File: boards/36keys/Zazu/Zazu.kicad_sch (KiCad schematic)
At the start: 169 parts, among them J1 Conn_01x12_Female, J2 Conn_01x12_Female, J3 Conn_01x08_Female, J4 Conn_01x08_Female, J5 Conn_01x03_Female, SW1 SW_Push, SW10 SW_Push, SW11 SW_Push, SW12 SW_Push, SW13 SW_Push, SW14 SW_Push, SW15 SW_Push, SW16 SW_Push, SW17 SW_Push, SW18 SW_Push, SW19 SW_Push, SW2 SW_Push, SW20 SW_Push, SW21 SW_Push, SW22 SW_Push, SW23 SW_Push, SW24 SW_Push, SW25 SW_Push, SW26 SW_Push, SW27 SW_Push, SW28 SW_Push, SW29 SW_Push, SW3 SW_Push, SW30 SW_Push, SW31 SW_Push, SW32 SW_Push, SW33 SW_Push, SW34 SW_Push, SW35 SW_Push, SW36 RotaryEncoder, SW37 SW_SPDT, SW38 SW_Push, SW39 SW_Push, SW4 SW_Push, SW40 SW_Push, SW41 SW_Push, SW42 SW_Push, SW43 SW_Push, SW44 SW_Push, SW45 SW_Push, SW46 SW_Push, SW5 SW_Push, SW6 SW_Push, SW7 SW_Push, SW8 SW_Push, SW9 SW_Push, U1 Elite-C, U2 74HC595, U3 TCR2EF19,LM(CT, U4 PMW3360DM-T2QU, U5 DRV2605L

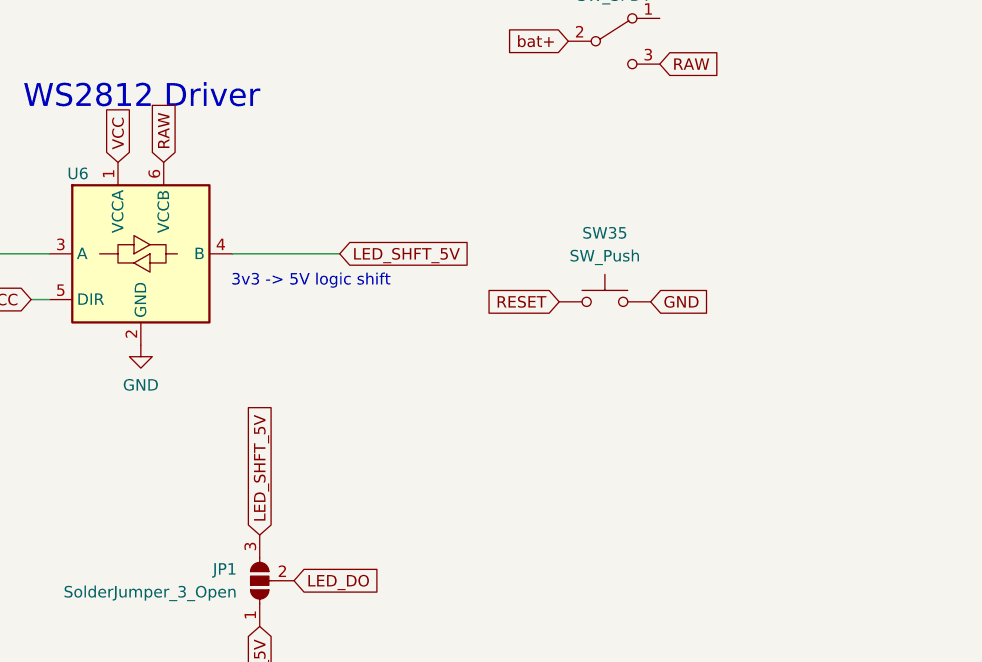
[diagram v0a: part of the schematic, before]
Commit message: change Zazu's reset switch
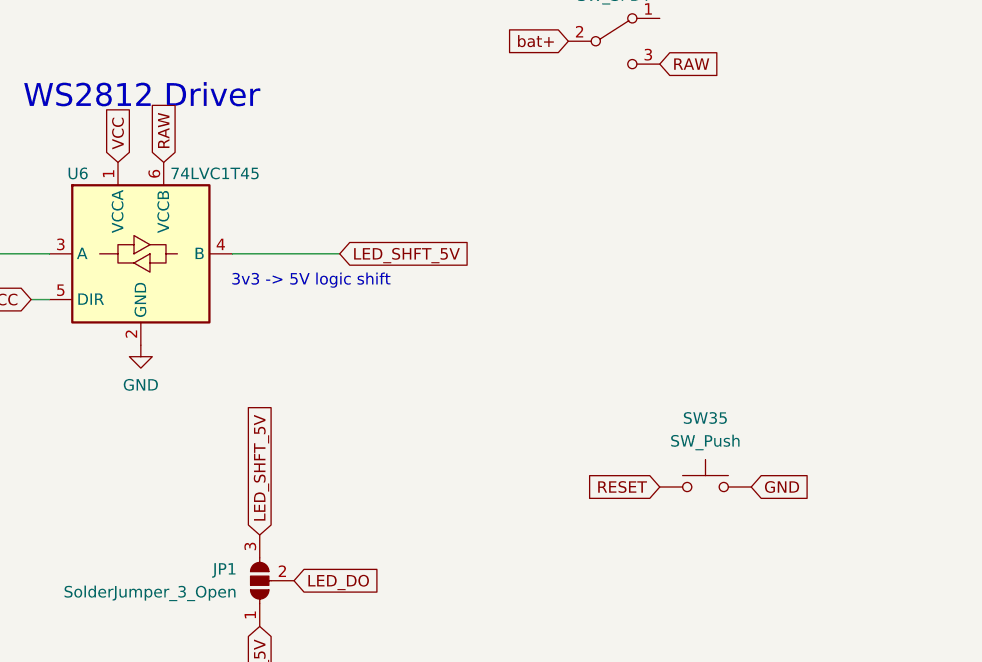
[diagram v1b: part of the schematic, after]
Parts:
- SW35: footprint Button_Switch_SMD:SW_SPST_Omron_B3FS-100xP -> Alaa:SKQG-1155865; LCSC C271750 -> C221856
- U6: value (none) -> 74LVC1T45; footprint (none) -> Package_TO_SOT_SMD:SOT-363_SC-70-6
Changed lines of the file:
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@@
     )
   )
+  (global_label "RESET" (shape input) (at 384.81 257.556 180) (fields_autoplaced)
+    (effects (font (size 1.27 1.27)) (justify right))
+    (property "Intersheet References" "${INTERSHEET_REFS}" (id 0) (at 376.6517 257.4766 0)
+      (effects (font (size 1.27 1.27)) (justify right) hide)
+    )
+  )
   (global_label "SCL" (shape input) (at 360.426 114.554 180) (fields_autoplaced)
     (effects (font (size 1.27 1.27)) (justify right))
@@
     )
   )
-  (global_label "GND" (shape input) (at 383.794 236.982 0) (fields_autoplaced)
-    (effects (font (size 1.27 1.27)) (justify left))
-    (property "Intersheet References" "${INTERSHEET_REFS}" (id 0) (at 390.0776 236.9026 0)
-      (effects (font (size 1.27 1.27)) (justify left) hide)
-    )
-  )
   (global_label "VCC" (shape input) (at 360.426 109.474 180) (fields_autoplaced)
     (effects (font (size 1.27 1.27)) (justify right))
@@
     )
   )
+  (global_label "GND" (shape input) (at 394.97 257.556 0) (fields_autoplaced)
+    (effects (font (size 1.27 1.27)) (justify left))
+    (property "Intersheet References" "${INTERSHEET_REFS}" (id 0) (at 401.2536 257.4766 0)
+      (effects (font (size 1.27 1.27)) (justify left) hide)
+    )
+  )
   (global_label "LED_SHFT_5V" (shape input) (at 349.25 231.648 0) (fields_autoplaced)
     (effects (font (size 1.27 1.27)) (justify left))
@@
     )
   )
-  (global_label "RESET" (shape input) (at 373.634 236.982 180) (fields_autoplaced)
-    (effects (font (size 1.27 1.27)) (justify right))
-    (property "Intersheet References" "${INTERSHEET_REFS}" (id 0) (at 365.4757 236.9026 0)
-      (effects (font (size 1.27 1.27)) (justify right) hide)
-    )
-  )
   (symbol (lib_id "alaa:Diode_1N4148") (at 63.5 48.26 270) (unit 1)
     (in_bom yes) (on_board yes) (fields_autoplaced)
@@
     (in_bom yes) (on_board yes)
     (property "Reference" "U6" (id 0) (at 320.167 222.758 0))
-    (property "Value" "" (id 1) (at 335.407 222.758 0))
-    (property "Footprint" "" (id 2) (at 327.152 243.078 0)
+    (property "Value" "74LVC1T45" (id 1) (at 335.407 222.758 0))
+    (property "Footprint" "Package_TO_SOT_SMD:SOT-363_SC-70-6" (id 2) (at 327.152 243.078 0)
       (effects (font (size 1.27 1.27)) hide)
     )
@@
     (pin "2")
   )
-  (symbol (lib_id "Switch:SW_Push") (at 378.714 236.982 0) (unit 1)
-    (in_bom yes) (on_board yes) (fields_autoplaced)
-    (property "Reference" "SW35" (id 0) (at 378.714 229.362 0))
-    (property "Value" "SW_Push" (id 1) (at 378.714 231.902 0))
-    (property "Footprint" "Button_Switch_SMD:SW_SPST_Omron_B3FS-100xP" (id 2) (at 378.714 231.902 0)
-      (effects (font (size 1.27 1.27)) hide)
-    )
-    (property "Datasheet" "~" (id 3) (at 378.714 231.902 0)
-      (effects (font (size 1.27 1.27)) hide)
-    )
-    (property "LCSC" "C271750" (id 4) (at 378.714 236.982 0)
-      (effects (font (size 1.27 1.27)) hide)
-    )
-    (pin "1")
-    (pin "2")
-  )
   (symbol (lib_id "alaa:Diode_1N4148") (at 124.46 128.27 270) (unit 1)
     (in_bom yes) (on_board yes) (fields_autoplaced)
@@
     (pin "1")
   )
+  (symbol (lib_id "Switch:SW_Push") (at 389.89 257.556 0) (unit 1)
+    (in_bom yes) (on_board yes) (fields_autoplaced)
+    (property "Reference" "SW35" (id 0) (at 389.89 249.936 0))
+    (property "Value" "SW_Push" (id 1) (at 389.89 252.476 0))
+    (property "Footprint" "Alaa:SKQG-1155865" (id 2) (at 389.89 252.476 0)
+      (effects (font (size 1.27 1.27)) hide)
+    )
+    (property "Datasheet" "~" (id 3) (at 389.89 252.476 0)
+      (effects (font (size 1.27 1.27)) hide)
+    )
+    (property "LCSC" "C221856" (id 4) (at 389.89 257.556 0)
+      (effects (font (size 1.27 1.27)) hide)
+    )
+    (pin "1")
+    (pin "2")
+  )
   (symbol (lib_id "alaa:Diode_1N4148") (at 154.94 101.6 270) (unit 1)
     (in_bom yes) (on_board yes) (fields_autoplaced)
@@
       (reference "SW34") (unit 1) (value "SW_Push") (footprint "Alaa:Kailh_hotswap_only_MX-CHOC")
     )
-    (path "/3a43c328-e467-4d29-aba9-46dbfa9652ed"
-      (reference "SW35") (unit 1) (value "SW_Push") (footprint "Button_Switch_SMD:SW_SPST_Omron_B3FS-100xP")
+    (path "/5fdbeecb-600c-4689-a92f-7820269d7655"
+      (reference "SW35") (unit 1) (value "SW_Push") (footprint "Alaa:SKQG-1155865")
     )
     (path "/9c465d0a-3acf-44e4-926b-a8e6ae8ccd7b"

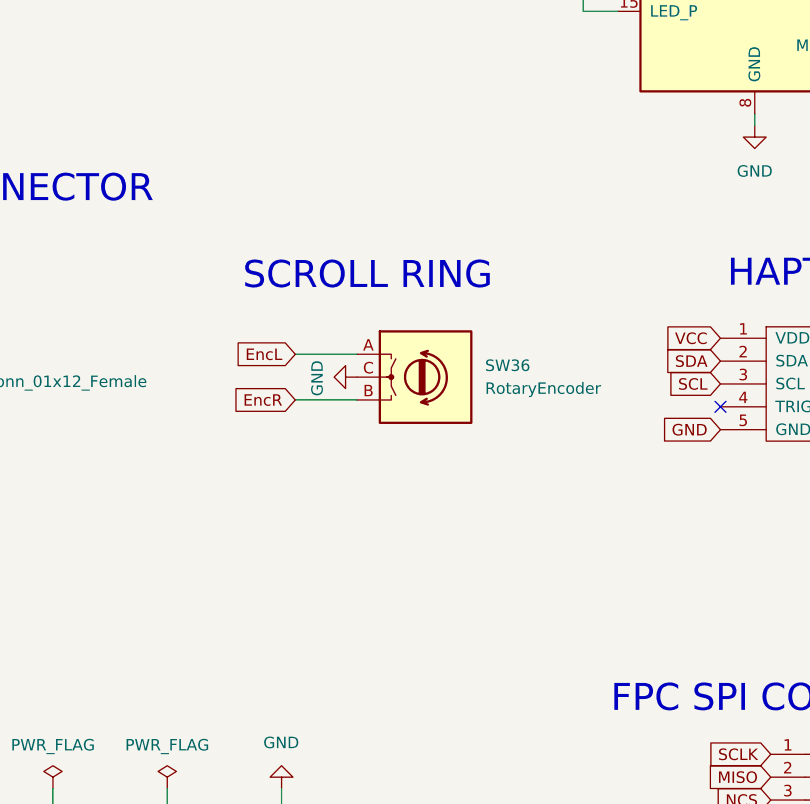
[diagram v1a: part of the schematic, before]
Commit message: add resistors to scroll ring circuit
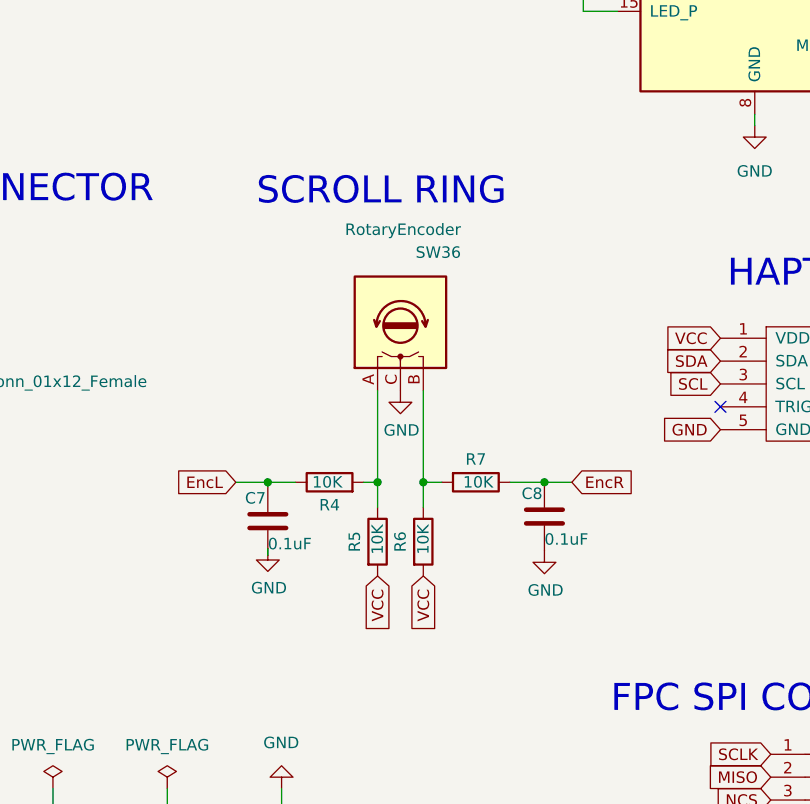
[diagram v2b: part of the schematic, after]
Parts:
- added C7, C8: 0.1uF, Capacitor_SMD:C_0805_2012Metric, symbol Device:C
- added R4, R5, R6, R7: 10K, Resistor_SMD:R_0805_2012Metric, symbol Device:R
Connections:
- net EncL: now also C7.1, R4.1; no longer SW36.A
- net EncR: now also C8.1, R7.1; no longer SW36.B
- net GND: now also C7.2, C8.2
- net VCC: now also R5.2, R6.2
- new net: R6.1, R7.2, SW36.B
- new net: R4.2, R5.1, SW36.A
